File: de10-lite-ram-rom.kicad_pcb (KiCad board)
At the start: 2 copper layers, 50.8 x 31.8 mm, 15 parts, among them J1 Conn_02x20_Odd_Even, U1 IS61C5128AS-25TLI, U2 SST39SF040, U3 74LVC2G04

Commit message: fixed labels, tracks, created gerbers
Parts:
- J1: value Conn_02x20_Odd_Even -> DE10-Lite GPIO
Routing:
- net GND: track 6.90 -> 1.54 mm, vias 46 -> 49
- net /D1: track 42.9 -> 46.6 mm, vias 3 -> 2
- net VCC: track 163.1 -> 160.1 mm
- net /D4: track 33.0 -> 35.9 mm
- net /D0: track 39.8 -> 41.5 mm
- net /A17: track 67.1 -> 68.6 mm
- net /A14: track 70.3 -> 71.3 mm
- net /D2: track 43.3 -> 42.6 mm
- net /A18: track 41.9 -> 42.5 mm

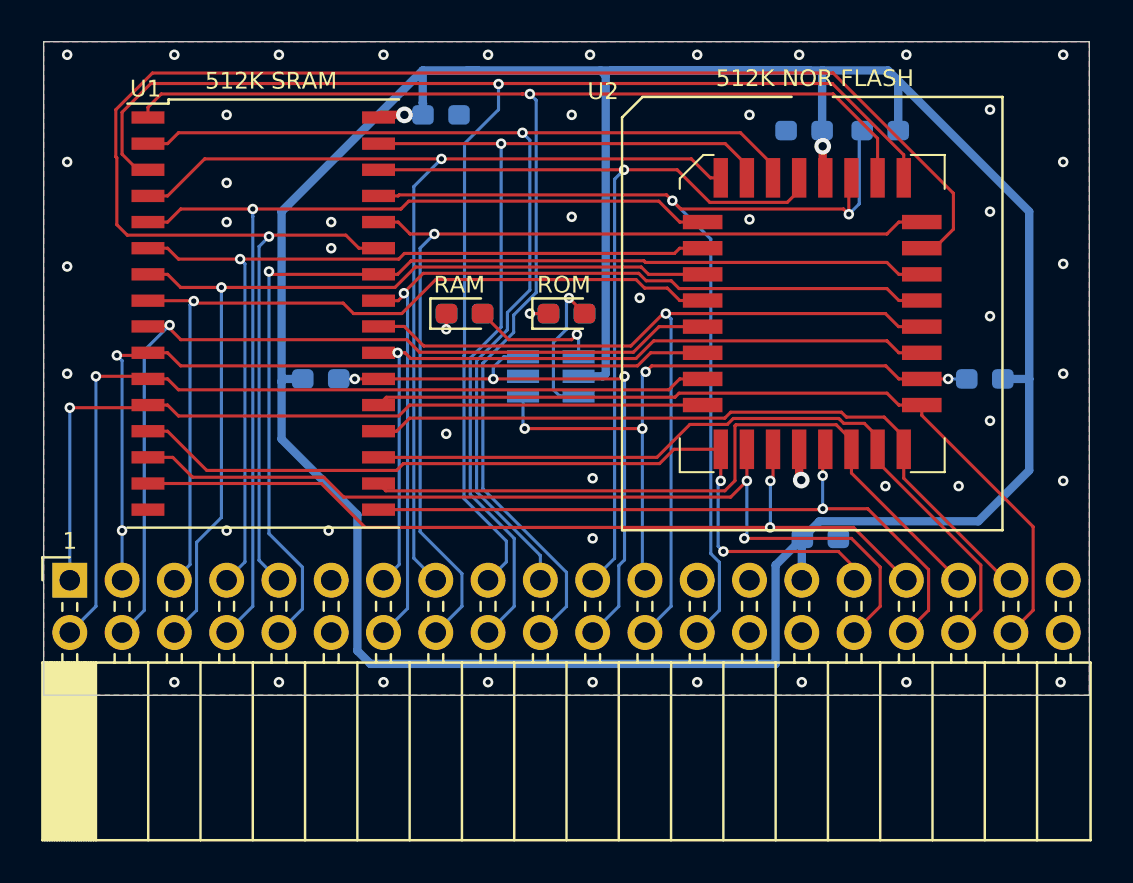
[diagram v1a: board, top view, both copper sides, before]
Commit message: fanned out power traces
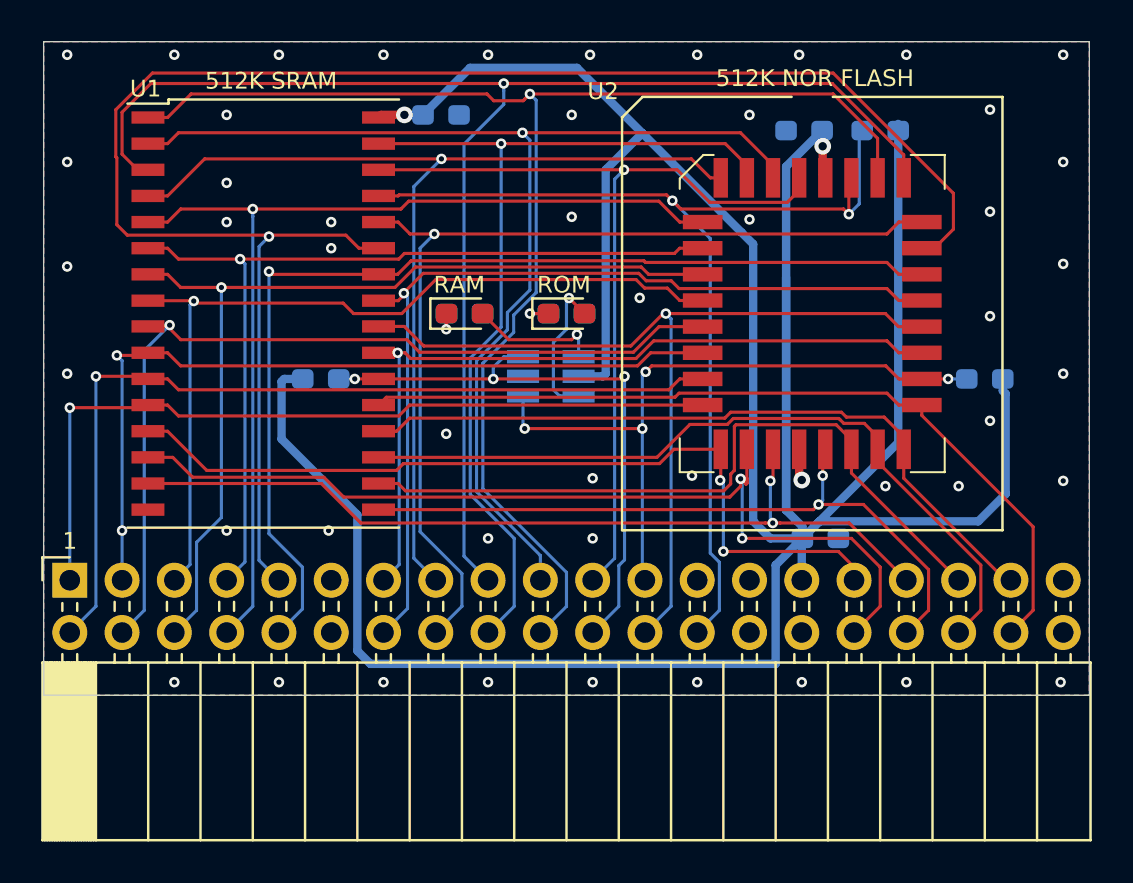
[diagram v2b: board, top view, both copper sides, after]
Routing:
- net VCC: track 160.1 -> 169.9 mm
- net /A14: track 71.3 -> 70.7 mm
- net GND: track 1.54 -> 1.55 mm, vias 49 -> 51

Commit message: version 1.0
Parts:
- C2: moved to F.Cu
- moved C2 0.25 mm to (140.2, 115.1)
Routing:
- net VCC: track 169.9 -> 13.5 mm, vias 2 -> 7
- net GND: track 1.55 -> 10.8 mm, vias 51 -> 49
- net /A14: track 70.7 -> 73.1 mm
- net /A2: track 40.1 -> 41.4 mm, vias 2 -> 1
- net /D1: track 47.0 -> 46.0 mm
- net /A1: track 42.9 -> 43.8 mm
- net /A15: track 44.7 -> 45.5 mm
- net /D6: track 35.7 -> 36.5 mm
- net /A0: track 39.6 -> 40.2 mm
- net /A7: track 48.9 -> 49.5 mm
- net /A10: track 38.5 -> 39.1 mm
- net /D7: track 40.6 -> 41.1 mm
- net Net-(D2-Pad2): track 6.33 -> 5.81 mm
- net Net-(D2-Pad1): track 1.54 -> 2.04 mm
- added copper zone on In1.Cu, net GND
- added copper zone on In2.Cu, net VCC
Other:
- copper layers 2 -> 4

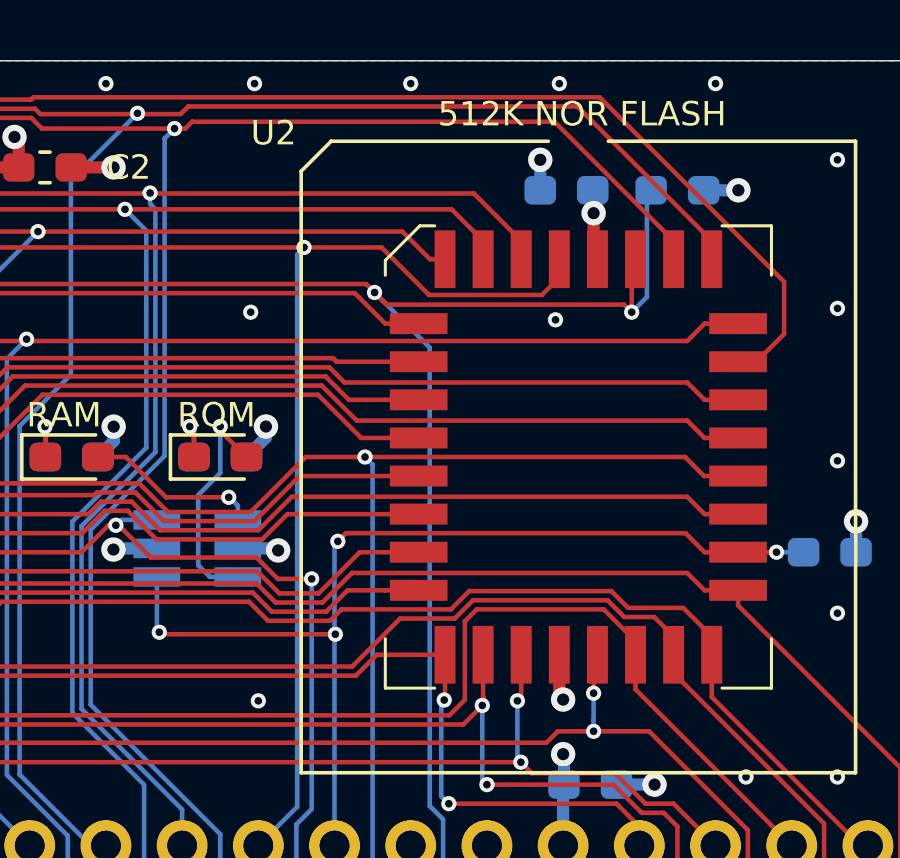
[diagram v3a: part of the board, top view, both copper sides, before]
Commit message: moved some traces around
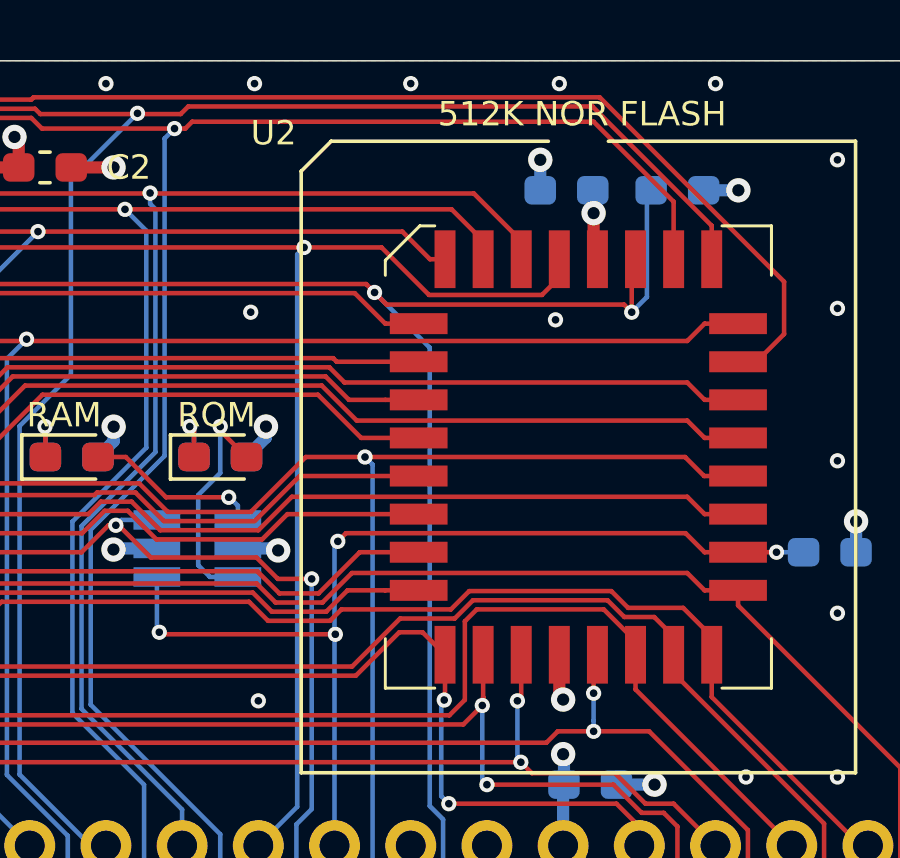
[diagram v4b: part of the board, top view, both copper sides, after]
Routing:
- net /A17: track 68.6 -> 69.4 mm
- net /D0: track 41.5 -> 42.1 mm
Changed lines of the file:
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@@
     (thickness 1.6)
     (drawings 10)
-    (tracks 564)
+    (tracks 565)
     (zones 0)
     (modules 15)
@@
   (page A4)
   (layers
-    (0 F.Cu signal hide)
+    (0 F.Cu signal)
     (1 In1.Cu signal hide)
-    (2 In2.Cu signal)
+    (2 In2.Cu signal hide)
     (31 B.Cu signal hide)
     (32 B.Adhes user hide)
@@
   (segment (start 160.02 137.033) (end 159.258 136.271) (width 0.1524) (layer F.Cu) (net 11) (status 10))
   (segment (start 160.02 137.668) (end 160.02 137.033) (width 0.1524) (layer F.Cu) (net 11) (status 30))
-  (segment (start 151.2685 131.3065) (end 153.543 131.3065) (width 0.1524) (layer F.Cu) (net 11) (status 20))
-  (segment (start 150.57119 132.00381) (end 151.2685 131.3065) (width 0.1524) (layer F.Cu) (net 11))
-  (segment (start 138.12519 132.00381) (end 150.57119 132.00381) (width 0.1524) (layer F.Cu) (net 11))
-  (segment (start 128.5754 132.334) (end 137.795 132.334) (width 0.1524) (layer F.Cu) (net 11))
-  (segment (start 137.795 132.334) (end 138.12519 132.00381) (width 0.1524) (layer F.Cu) (net 11))
-  (segment (start 126.6704 130.429) (end 128.5754 132.334) (width 0.1524) (layer F.Cu) (net 11))
-  (segment (start 125.718 130.429) (end 126.6704 130.429) (width 0.1524) (layer F.Cu) (net 11) (status 10))
   (segment (start 153.543 131.3065) (end 153.543 132.788042) (width 0.1524) (layer F.Cu) (net 11) (status 10))
   (via (at 153.516023 132.815019) (size 0.508) (drill 0.254) (layers F.Cu B.Cu) (net 11))
@@
   (segment (start 153.416 136.017) (end 153.416 132.915042) (width 0.1524) (layer B.Cu) (net 11))
   (segment (start 153.67 136.271) (end 153.416 136.017) (width 0.1524) (layer B.Cu) (net 11))
+  (segment (start 152.7925 130.556) (end 153.543 131.3065) (width 0.1524) (layer F.Cu) (net 11))
+  (segment (start 152.019 130.556) (end 152.7925 130.556) (width 0.1524) (layer F.Cu) (net 11))
+  (segment (start 128.5754 132.334) (end 137.795 132.334) (width 0.1524) (layer F.Cu) (net 11))
+  (segment (start 138.12519 132.00381) (end 150.57119 132.00381) (width 0.1524) (layer F.Cu) (net 11))
+  (segment (start 126.6704 130.429) (end 128.5754 132.334) (width 0.1524) (layer F.Cu) (net 11))
+  (segment (start 150.57119 132.00381) (end 152.019 130.556) (width 0.1524) (layer F.Cu) (net 11))
+  (segment (start 137.795 132.334) (end 138.12519 132.00381) (width 0.1524) (layer F.Cu) (net 11))
+  (segment (start 125.718 130.429) (end 126.6704 130.429) (width 0.1524) (layer F.Cu) (net 11))
   (via (at 159.766 119.888) (size 0.508) (drill 0.254) (layers F.Cu B.Cu) (net 12))
   (segment (start 159.766 118.2485) (end 159.893 118.1215) (width 0.1524) (layer F.Cu) (net 12) (status 30))
@@
   (segment (start 128.448402 113.410998) (end 139.750802 113.410998) (width 0.1524) (layer F.Cu) (net 17))
   (segment (start 125.718 115.189) (end 126.6704 115.189) (width 0.1524) (layer F.Cu) (net 17) (status 10))
-  (segment (start 161.163 118.1215) (end 161.163 117.509) (width 0.1524) (layer F.Cu) (net 17) (status 30))
-  (segment (start 144.885198 113.76661) (end 144.525988 113.76661) (width 0.1524) (layer F.Cu) (net 17))
   (segment (start 140.106414 113.76661) (end 144.525988 113.76661) (width 0.1524) (layer F.Cu) (net 17))
-  (segment (start 157.191988 113.537988) (end 145.11382 113.537988) (width 0.1524) (layer F.Cu) (net 17))
-  (segment (start 161.163 117.509) (end 157.191988 113.537988) (width 0.1524) (layer F.Cu) (net 17) (status 10))
   (segment (start 126.6704 115.189) (end 128.448402 113.410998) (width 0.1524) (layer F.Cu) (net 17))
   (segment (start 139.750802 113.410998) (end 140.106414 113.76661) (width 0.1524) (layer F.Cu) (net 17))
-  (segment (start 145.11382 113.537988) (end 144.885198 113.76661) (width 0.1524) (layer F.Cu) (net 17))
   (segment (start 144.194745 114.097853) (end 144.525988 113.76661) (width 0.1524) (layer B.Cu) (net 17))
   (segment (start 144.194745 124.67856) (end 144.194745 114.097853) (width 0.1524) (layer B.Cu) (net 17))
@@
   (segment (start 146.05 138.938) (end 146.05 137.287) (width 0.1524) (layer B.Cu) (net 17))
   (segment (start 144.78 140.208) (end 146.05 138.938) (width 0.1524) (layer B.Cu) (net 17))
+  (segment (start 144.885198 113.76661) (end 144.525988 113.76661) (width 0.1524) (layer F.Cu) (net 17))
+  (segment (start 158.495988 113.537988) (end 145.11382 113.537988) (width 0.1524) (layer F.Cu) (net 17))
+  (segment (start 161.163 116.205) (end 158.495988 113.537988) (width 0.1524) (layer F.Cu) (net 17))
+  (segment (start 145.11382 113.537988) (end 144.885198 113.76661) (width 0.1524) (layer F.Cu) (net 17))
+  (segment (start 161.163 118.1215) (end 161.163 116.205) (width 0.1524) (layer F.Cu) (net 17))
   (segment (start 154.504399 115.930399) (end 156.083 117.509) (width 0.1524) (layer F.Cu) (net 18) (status 20))
   (segment (start 126.6704 116.459) (end 127.199001 115.930399) (width 0.1524) (layer F.Cu) (net 18))
@@
   (segment (start 162.433 118.734) (end 162.433 118.1215) (width 0.1524) (layer F.Cu) (net 20) (status 30))
   (via (at 143.291209 113.25861) (size 0.508) (drill 0.254) (layers F.Cu B.Cu) (net 20))
-  (segment (start 157.954 113.03) (end 162.433 117.509) (width 0.1524) (layer F.Cu) (net 20) (status 20))
-  (segment (start 144.730764 113.284) (end 144.984764 113.03) (width 0.1524) (layer F.Cu) (net 20))
-  (segment (start 140.054871 113.284) (end 144.730764 113.284) (width 0.1524) (layer F.Cu) (net 20))
-  (segment (start 126.289331 113.106187) (end 139.877058 113.106187) (width 0.1524) (layer F.Cu) (net 20))
-  (segment (start 124.46 114.935518) (end 126.289331 113.106187) (width 0.1524) (layer F.Cu) (net 20))
-  (segment (start 139.877058 113.106187) (end 140.054871 113.284) (width 0.1524) (layer F.Cu) (net 20))
-  (segment (start 144.984764 113.03) (end 157.954 113.03) (width 0.1524) (layer F.Cu) (net 20))
-  (segment (start 125.718 117.729) (end 125.218 117.729) (width 0.1524) (layer F.Cu) (net 20) (status 30))
-  (segment (start 124.46 116.971) (end 124.46 114.935518) (width 0.1524) (layer F.Cu) (net 20))
-  (segment (start 162.433 117.509) (end 162.433 118.1215) (width 0.1524) (layer F.Cu) (net 20) (status 30))
-  (segment (start 125.218 117.729) (end 124.46 116.971) (width 0.1524) (layer F.Cu) (net 20) (status 10))
   (segment (start 141.071567 115.478252) (end 143.291209 113.25861) (width 0.1524) (layer B.Cu) (net 20))
   (segment (start 141.732 137.668) (end 139.361461 135.297461) (width 0.1524) (layer B.Cu) (net 20) (status 10))
@@
   (segment (start 139.361461 135.297461) (end 139.361461 123.684358) (width 0.1524) (layer B.Cu) (net 20))
   (segment (start 142.24 137.668) (end 141.732 137.668) (width 0.1524) (layer B.Cu) (net 20) (status 30))
+  (segment (start 144.984764 113.03) (end 158.4564 113.03) (width 0.1524) (layer F.Cu) (net 20))
+  (segment (start 144.730764 113.284) (end 144.984764 113.03) (width 0.1524) (layer F.Cu) (net 20))
+  (segment (start 139.877058 113.106187) (end 140.054871 113.284) (width 0.1524) (layer F.Cu) (net 20))
+  (segment (start 162.433 117.0066) (end 162.433 118.1215) (width 0.1524) (layer F.Cu) (net 20))
+  (segment (start 140.054871 113.284) (end 144.730764 113.284) (width 0.1524) (layer F.Cu) (net 20))
+  (segment (start 125.718 117.729) (end 125.218 117.729) (width 0.1524) (layer F.Cu) (net 20))
+  (segment (start 126.289331 113.106187) (end 139.877058 113.106187) (width 0.1524) (layer F.Cu) (net 20))
+  (segment (start 124.46 114.935518) (end 126.289331 113.106187) (width 0.1524) (layer F.Cu) (net 20))
+  (segment (start 124.46 116.971) (end 124.46 114.935518) (width 0.1524) (layer F.Cu) (net 20))
+  (segment (start 158.4564 113.03) (end 162.433 117.0066) (width 0.1524) (layer F.Cu) (net 20))
+  (segment (start 125.218 117.729) (end 124.46 116.971) (width 0.1524) (layer F.Cu) (net 20))
   (segment (start 138.449001 120.847601) (end 161.616999 120.847601) (width 0.1524) (layer F.Cu) (net 21))
   (segment (start 161.616999 120.847601) (end 162.1956 120.269) (width 0.1524) (layer F.Cu) (net 21))
